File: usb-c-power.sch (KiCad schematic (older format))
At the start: 22 parts

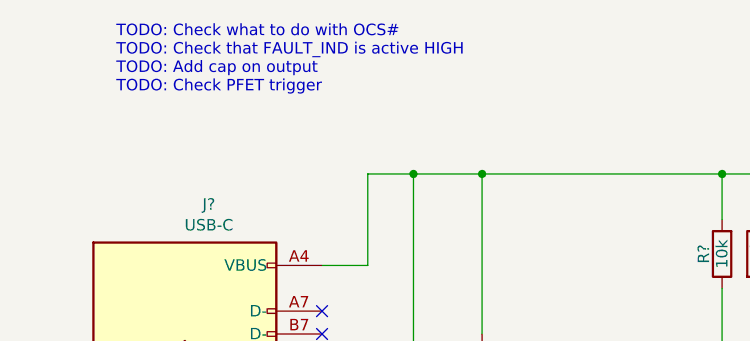
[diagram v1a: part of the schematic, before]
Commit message: update schematic after LTSpice simulations
- enable EN/UV and PGFB usage for LDOs
  - PGFB required for fast startup
  - EN/UV required to allow boost to ramp up
- take care of some TODOs in usbc-power sch
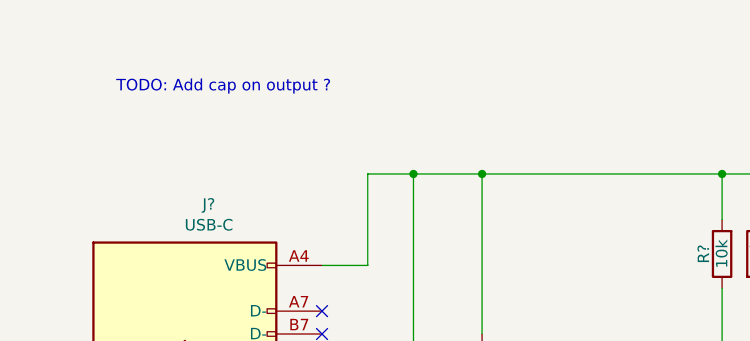
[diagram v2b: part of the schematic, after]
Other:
- note added: "TODO: Add cap on output ?"
- note removed: "TODO: Check what to do with OCS#\nTODO: Check that FAULT_IND is active HIGH\nTODO: Add cap on output\nTODO: Check PFET trigger"
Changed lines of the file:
@@
 NoConn ~ 5350 4100
 Text Notes 2400 2500 0    50   ~ 0
-TODO: Check what to do with OCS#\nTODO: Check that FAULT_IND is active HIGH\nTODO: Add cap on output\nTODO: Check PFET trigger
+TODO: Add cap on output ?
 Wire Wire Line
 	8650 3150 8650 3550

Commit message: replace USB Type-C connector
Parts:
- J?: footprint amphenol:USB_C_Receptacle_Amphenol_12401598E4-2A -> amphenol:USB_C_Receptacle_Amphenol_12401610E4-2A_CircularHoles; Description CONN RCPT USB3.1 TYPEC SMD R/A -> CONN RCP USB3.1 TYPEC 24P SMD RA; Manufacturer Amphenol Commercial Products -> Amphenol ICC (Commercial Products); Manufacturer Part Number 12401598E4#2A -> 12401610E4#2A; Supplier Part Number 12401598E4#2ACT-ND -> 12401610E4#2ACT-ND
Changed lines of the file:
@@
 F 0 "J?" H 2805 4717 50  0000 C CNN
 F 1 "USB-C" H 2805 4626 50  0000 C CNN
-F 2 "amphenol:USB_C_Receptacle_Amphenol_12401598E4-2A" H 2850 3850 50  0001 C CNN
-F 3 "https://www.amphenol-icc.com/media/wysiwyg/files/drawing/12401598xxx2a.pdf" H 2850 3850 50  0001 C CNN
-F 4 "CONN RCPT USB3.1 TYPEC SMD R/A" H -150 -50 50  0001 C CNN "Description"
-F 5 "Amphenol Commercial Products" H -150 -50 50  0001 C CNN "Manufacturer"
-F 6 "12401598E4#2A" H -150 -50 50  0001 C CNN "Manufacturer Part Number"
+F 2 "amphenol:USB_C_Receptacle_Amphenol_12401610E4-2A_CircularHoles" H 2850 3850 50  0001 C CNN
+F 3 "https://www.amphenol-icc.com/media/wysiwyg/files/drawing/12401610e4x2a.pdf" H 2850 3850 50  0001 C CNN
+F 4 "CONN RCP USB3.1 TYPEC 24P SMD RA" H -150 -50 50  0001 C CNN "Description"
+F 5 "Amphenol ICC (Commercial Products)" H -150 -50 50  0001 C CNN "Manufacturer"
+F 6 "12401610E4#2A" H -150 -50 50  0001 C CNN "Manufacturer Part Number"
 F 7 "Digi-Key" H -150 -50 50  0001 C CNN "Supplier"
-F 8 "12401598E4#2ACT-ND" H -150 -50 50  0001 C CNN "Supplier Part Number"
+F 8 "12401610E4#2ACT-ND" H -150 -50 50  0001 C CNN "Supplier Part Number"
 	1    2700 3850
 	1    0    0    -1
